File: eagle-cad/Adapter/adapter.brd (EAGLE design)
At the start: 55.8 x 65.1 mm, 19 parts, among them M1 WIREPADSMD5-2,5, M2 WIREPADSMD5-2,5, M3 WIREPADSMD5-2,5, M4 WIREPADSMD5-2,5

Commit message: Worked on Adapter
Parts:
- removed GND2, GND3, GND4, M1, M2, M3, M4, VBAT1, VBAT2, VBAT3, VBAT4: WIREPADSMD5-2,5, wirepad:5-2,5
- removed J4: (no value), SparkFun-Connectors:1X05_NO_SILK
- removed J5: (no value), SparkFun-Connectors:1X03_NO_SILK
- moved GND1 47.0 mm to (18.8, 5.10), turned to 180 degrees
- moved J1 26.1 mm to (18.7, 44.0), flipped to the bottom
- moved J2 22.4 mm to (34.0, 44.0), flipped to the bottom
- moved J3 9.87 mm to (33.2, 15.9), turned to 270 degrees
- moved VBAT 6.10 mm to (28.2, 5.03)
- moved GND 0.36 mm to (35.1, 5.14)
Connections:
- new net SBUS: GND1.1
- net 3V3: no longer J4.4
- net 5V: no longer J5.1
- net GND: no longer GND1.1, GND2.1, GND3.1, GND4.1, J4.5, J5.2
- net M1: no longer M1.1
- net M2: no longer M2.1
- net M3: no longer M3.1
- net M4: no longer M4.1
- net RX1: no longer J5.3
- net SCL: no longer J4.2
- net SDA: no longer J4.1
- net VBAT: no longer VBAT1.1, VBAT2.1, VBAT3.1, VBAT4.1
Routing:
- net VBAT: track 120.6 -> 0.00 mm
- net 5V: track 73.9 -> 0.14 mm, vias 1 -> 0
- net 3V3: track 50.5 -> 0.00 mm, vias 1 -> 0
- net M3: track 48.3 -> 0.00 mm, vias 1 -> 0
- net GND: track 46.8 -> 0.00 mm, vias 1 -> 0
- net M4: track 42.1 -> 0.00 mm, vias 1 -> 0
- net SDA: track 39.1 -> 0.00 mm
- net SCL: track 36.1 -> 0.00 mm
- net M1: track 29.6 -> 0.00 mm, vias 1 -> 0
- net RX1: track 16.4 -> 0.00 mm
- net M2: track 14.5 -> 0.00 mm, vias 1 -> 0
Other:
- board size 55.8 x 65.1 mm -> 34.5 x 48.1 mm
- board text removed: "+"
- board text removed: "3V3"
- board text removed: "5V"
- board text removed: "M1"
- board text removed: "M2"
- board text removed: "M3"
- board text removed: "M4"
- board text removed: "RX1"
- board text removed: "SCL"
- board text removed: "SDA"

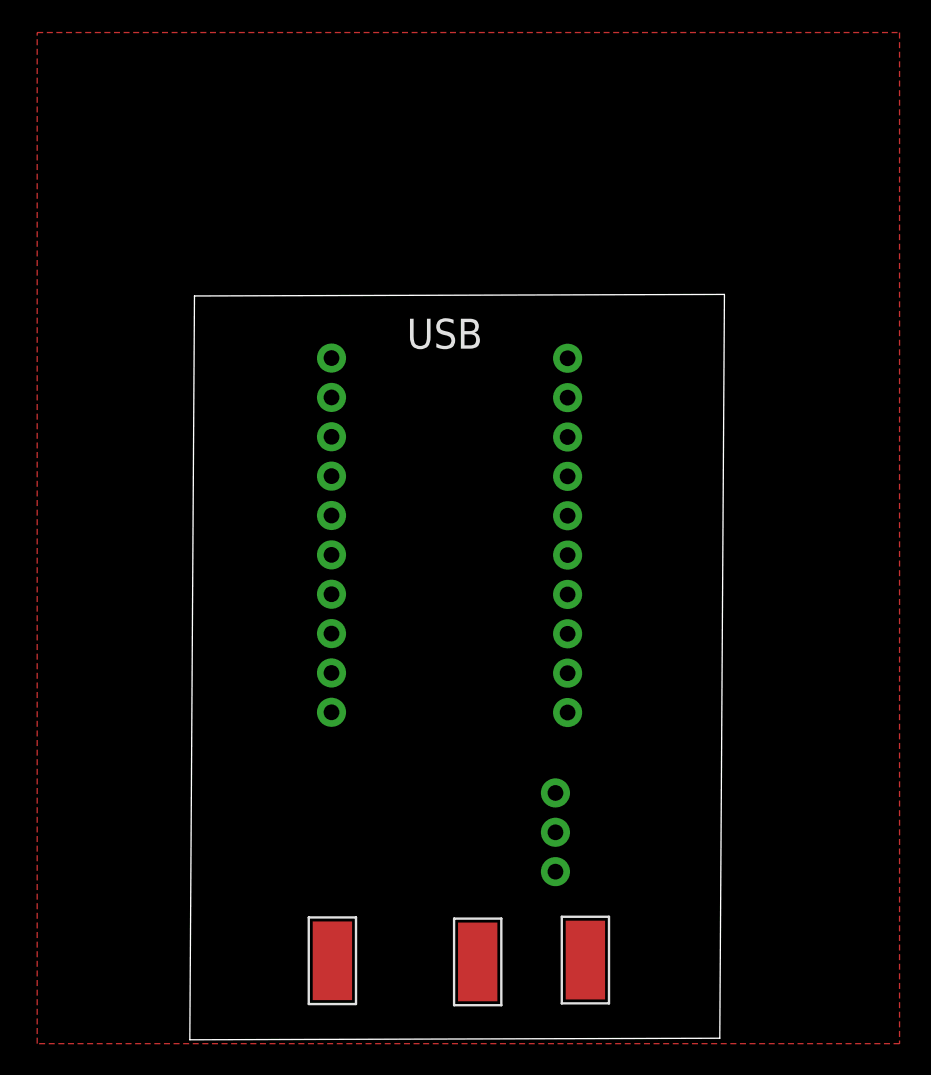
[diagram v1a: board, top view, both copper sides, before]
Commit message: Finished Taranis X-Lite adapter design
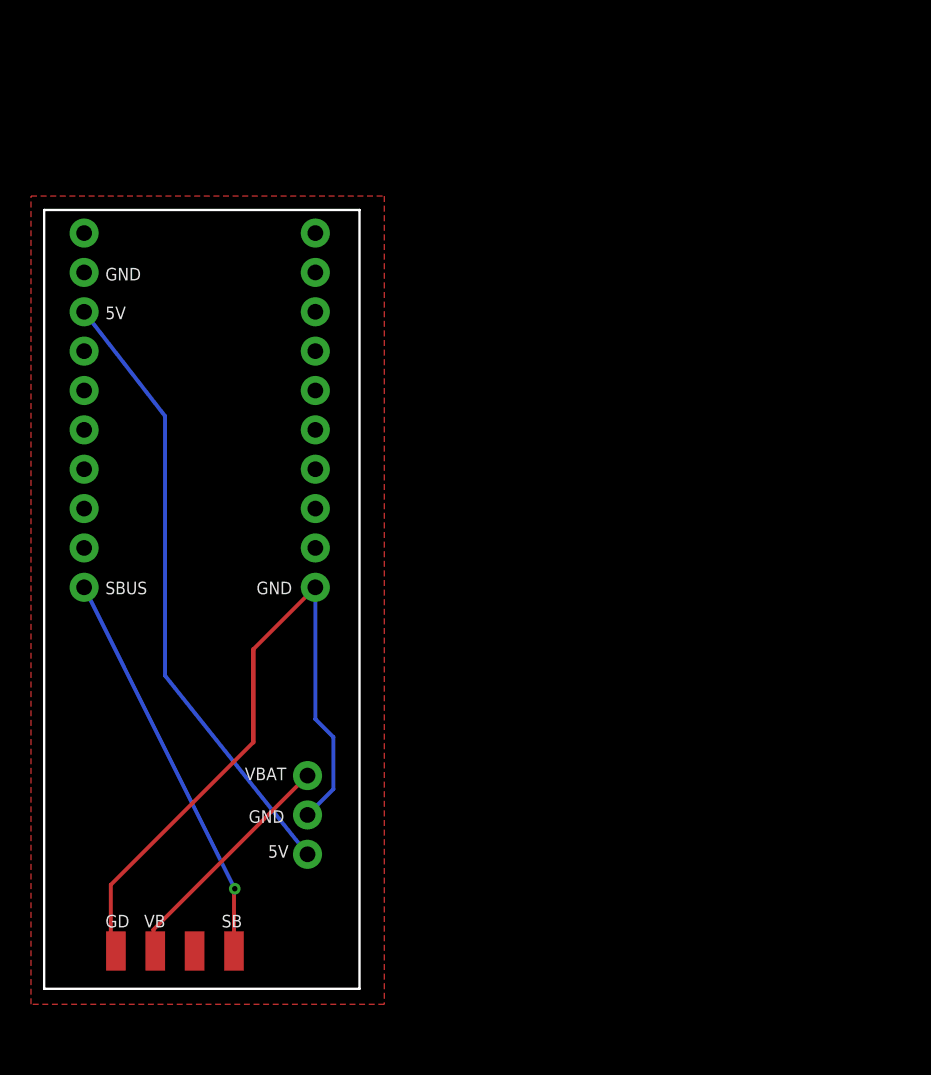
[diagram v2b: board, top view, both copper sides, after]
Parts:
- removed GND1: WIREPADSMD5-2,5, wirepad:5-2,5
- added PAD1, SBUS: (no value), wirepad:SMD1,27-2,54
- GND, VBAT: value WIREPADSMD5-2,5 -> (none); device wirepad:5-2,5 -> wirepad:SMD1,27-2,54
- moved J2 34.5 mm to (2.78, 29.2), turned to 90 degrees
- moved GND 30.3 mm to (4.83, 5.73)
- moved VBAT 20.8 mm to (7.37, 5.73)
- moved J3 16.5 mm to (17.2, 12.0), turned to 90 degrees
- moved J1 14.8 mm to (17.7, 29.2), turned to 90 degrees
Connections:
- removed net M1: J1.10
- removed net M4: J1.7
- removed net MISO: J2.2
- removed net MOSI: J2.1
- removed net RX1: J2.7
- removed net SCK: J2.3
- removed net SCL: J2.5
- removed net SDA: J2.6
- removed net SS: J2.4
- removed net TX1: J2.8
- net 5V: now also J2.8; no longer J1.3
- net GND: now also J1.1, J2.9; no longer J1.2, J2.10
- net SBUS: now also J2.1, SBUS.1; no longer GND1.1
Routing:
- net GND: track 0.00 -> 44.9 mm
- net 5V: track 0.14 -> 40.0 mm
- net SBUS: track 0.00 -> 26.3 mm, vias 0 -> 1
- net VBAT: track 0.00 -> 14.9 mm
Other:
- board size 34.5 x 48.1 mm -> 20.4 x 50.3 mm
- board text added: "5V"
- board text added: "GD"
- board text added: "GND"
- board text added: "SB"
- board text added: "SBUS"
- board text added: "VB"
- board text added: "VBAT"
- board text removed: "-"
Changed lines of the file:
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@@
 <?xml version="1.0" encoding="utf-8"?>
 <!DOCTYPE eagle SYSTEM "eagle.dtd">
-<eagle version="9.6.2">
+<eagle version="9.1.1">
 <drawing>
 <settings>
@@
 <setting verticaltext="up"/>
 </settings>
-<grid distance="0.1" unitdist="mm" unit="mm" style="lines" multiple="1" display="no" altdistance="5" altunitdist="mil" altunit="mil"/>
+<grid distance="9.84251969" unitdist="mil" unit="mil" style="lines" multiple="1" display="no" altdistance="5" altunitdist="mil" altunit="mil"/>
 <layers>
 <layer number="1" name="Top" color="4" fill="1" visible="yes" active="yes"/>
@@
 <board>
 <plain>
-<wire x1="9.6" y1="0" x2="43.8" y2="0.1" width="0" layer="20"/>
-<wire x1="43.8" y1="0.1" x2="44.1" y2="48.1" width="0" layer="20"/>
-<wire x1="44.1" y1="48.1" x2="9.9" y2="48" width="0" layer="20"/>
-<wire x1="9.9" y1="48" x2="9.6" y2="0" width="0" layer="20"/>
-<text x="23.6" y="44.6" size="1.9304" layer="25">USB</text>
-<text x="32.6" y="20.2" size="2.54" layer="26" rot="MR0">-</text>
+<text x="13.45" y="50.25" size="1.9304" layer="26" rot="MR0">USB</text>
+<wire x1="0.2" y1="53.55" x2="20.55" y2="53.55" width="0.1524" layer="20"/>
+<wire x1="20.55" y1="53.55" x2="20.55" y2="3.29" width="0.1524" layer="20"/>
+<wire x1="20.55" y1="3.29" x2="0.2" y2="3.29" width="0.1524" layer="20"/>
+<wire x1="0.2" y1="3.29" x2="0.2" y2="53.55" width="0.1524" layer="20"/>
+<text x="16.4" y="28.75" size="0.8128" layer="26" rot="MR0">GND</text>
+<text x="15.9" y="11.75" size="0.8128" layer="26" rot="MR0">5V</text>
+<text x="15.9" y="14" size="0.8128" layer="26" rot="MR0">GND</text>
+<text x="15.9" y="16.75" size="0.8128" layer="26" rot="MR0">VBAT</text>
+<text x="4.15" y="7.25" size="0.8128" layer="25">GD</text>
+<text x="6.65" y="7.25" size="0.8128" layer="25">VB</text>
+<text x="11.65" y="7.25" size="0.8128" layer="25">SB</text>
+<text x="4.15" y="28.75" size="0.8128" layer="25">SBUS</text>
+<text x="13.15" y="16.75" size="0.8128" layer="25">VBAT</text>
+<text x="13.4" y="14" size="0.8128" layer="25">GND</text>
+<text x="14.65" y="11.75" size="0.8128" layer="25">5V</text>
+<text x="4.15" y="46.5" size="0.8128" layer="25">5V</text>
+<text x="5.4" y="46.5" size="0.8128" layer="26" rot="MR0">5V</text>
+<text x="6.65" y="49" size="0.8128" layer="26" rot="MR0">GND</text>
+<text x="4.15" y="49" size="0.8128" layer="25">GND</text>
+<text x="13.9" y="28.75" size="0.8128" layer="25">GND</text>
+<text x="7.15" y="28.75" size="0.8128" layer="26" rot="MR0">SBUS</text>
 </plain>
 <attributes>
@@
 </autorouter>
 <elements>
-<element name="GND" library="wirepad" package="5-2,5" value="WIREPADSMD5-2,5" x="35.127490625" y="5.1442875" smashed="yes">
-<attribute name="VALUE" x="35.027490625" y="7.9442875" size="0.0254" layer="27"/>
-</element>
-<element name="VBAT" library="wirepad" package="5-2,5" value="WIREPADSMD5-2,5" x="28.177490625" y="5.02508125" smashed="yes">
-<attribute name="VALUE" x="28.077490625" y="7.82508125" size="0.0254" layer="27"/>
-</element>
-<element name="J1" library="SparkFun-Connectors" package="1X10_NO_SILK" value="" x="18.743490625" y="43.993071875" smashed="yes" rot="MR270">
-<attribute name="VALUE" x="20.775490625" y="45.263071875" size="0.6096" layer="28" font="vector" ratio="20" rot="MR270"/>
-</element>
-<element name="J2" library="SparkFun-Connectors" package="1X10_NO_SILK" value="" x="33.979040625" y="43.97908125" smashed="yes" rot="MR270">
-<attribute name="VALUE" x="36.011040625" y="45.24908125" size="0.6096" layer="28" font="vector" ratio="20" rot="MR270"/>
-</element>
-<element name="J3" library="SparkFun-Connectors" package="1X03_NO_SILK" value="" x="33.195209375" y="15.92935625" smashed="yes" rot="R270">
-<attribute name="VALUE" x="31.163209375" y="17.19935625" size="0.6096" layer="27" font="vector" ratio="20" rot="R270"/>
-</element>
-<element name="GND1" library="wirepad" package="5-2,5" value="WIREPADSMD5-2,5" x="18.8" y="5.1" smashed="yes" rot="R180">
-<attribute name="VALUE" x="18.9" y="2.3" size="0.0254" layer="27" rot="R180"/>
+<element name="J1" library="SparkFun-Connectors" package="1X10_NO_SILK" value="" x="17.7" y="29.2" smashed="yes" rot="MR90">
+<attribute name="VALUE" x="15.668" y="27.93" size="0.6096" layer="28" font="vector" ratio="20" rot="MR90"/>
+</element>
+<element name="J2" library="SparkFun-Connectors" package="1X10_NO_SILK" value="" x="2.779040625" y="29.2" smashed="yes" rot="MR90">
+<attribute name="VALUE" x="0.747040625" y="27.93" size="0.6096" layer="28" font="vector" ratio="20" rot="MR90"/>
+</element>
+<element name="J3" library="SparkFun-Connectors" package="1X03_NO_SILK" value="" x="17.195209375" y="11.96935625" smashed="yes" rot="R90">
+<attribute name="VALUE" x="19.227209375" y="10.69935625" size="0.6096" layer="27" font="vector" ratio="20" rot="R90"/>
+</element>
+<element name="GND" library="wirepad" package="SMD1,27-2,54" value="" x="4.83" y="5.73" smashed="yes">
+<attribute name="VALUE" x="4.83" y="5.73" size="0.0254" layer="27"/>
+</element>
+<element name="VBAT" library="wirepad" package="SMD1,27-2,54" value="" x="7.37" y="5.73" smashed="yes">
+<attribute name="VALUE" x="7.37" y="5.73" size="0.0254" layer="27"/>
+</element>
+<element name="SBUS" library="wirepad" package="SMD1,27-2,54" value="" x="12.45" y="5.73" smashed="yes">
+<attribute name="VALUE" x="12.45" y="5.73" size="0.0254" layer="27"/>
+</element>
+<element name="PAD1" library="wirepad" package="SMD1,27-2,54" value="" x="9.91" y="5.73" smashed="yes">
+<attribute name="VALUE" x="9.91" y="5.73" size="0.0254" layer="27"/>
 </element>
 </elements>
@@
 <signal name="GND">
 <polygon width="0.1524" layer="1">
-<vertex x="-0.25" y="65"/>
-<vertex x="55.4" y="65"/>
-<vertex x="55.4" y="-0.25"/>
-<vertex x="-0.25" y="-0.25"/>
+<vertex x="-0.65" y="54.45"/>
+<vertex x="22.15" y="54.45"/>
+<vertex x="22.15" y="2.29"/>
+<vertex x="-0.65" y="2.29"/>
 </polygon>
-<contactref element="J1" pad="2"/>
-<contactref element="J2" pad="10"/>
 <contactref element="J3" pad="2"/>
 <contactref element="GND" pad="1"/>
-<wire x1="33.979040625" y1="21.11908125" x2="18.743490625" y2="41.453071875" width="0" layer="19" extent="1-1"/>
-<wire x1="33.195209375" y1="13.38935625" x2="33.979040625" y2="21.11908125" width="0" layer="19" extent="1-1"/>
-<wire x1="35.127490625" y1="5.1442875" x2="33.195209375" y2="13.38935625" width="0" layer="19" extent="1-1"/>
+<contactref element="J1" pad="1"/>
+<contactref element="J2" pad="9"/>
+<wire x1="17.7" y1="29.2" x2="17.7" y2="20.6969375" width="0.254" layer="16"/>
+<wire x1="17.7" y1="20.6969375" x2="18.8636125" y2="19.533325" width="0.254" layer="16"/>
+<wire x1="18.8636125" y1="19.533325" x2="18.8636125" y2="16.177759375" width="0.254" layer="16"/>
+<wire x1="18.8636125" y1="16.177759375" x2="17.195209375" y2="14.50935625" width="0.254" layer="16"/>
+<wire x1="13.7" y1="25.2" x2="13.7" y2="19.2" width="0.3048" layer="1"/>
+<wire x1="13.7" y1="19.2" x2="4.5" y2="10" width="0.254" layer="1"/>
+<wire x1="4.5" y1="10" x2="4.5" y2="6.06" width="0.254" layer="1"/>
+<wire x1="4.5" y1="6.06" x2="4.83" y2="5.73" width="0.1524" layer="1"/>
+<wire x1="17.7" y1="29.2" x2="13.7" y2="25.2" width="0.254" layer="1"/>
 </signal>
 <signal name="5V">
-<contactref element="J1" pad="3"/>
 <contactref element="J3" pad="1"/>
-<wire x1="18.743490625" y1="38.913071875" x2="18.843490625" y2="39.013071875" width="0.1524" layer="16"/>
-<wire x1="33.195209375" y1="15.92935625" x2="18.743490625" y2="38.913071875" width="0" layer="19" extent="1-1"/>
+<contactref element="J2" pad="8"/>
+<wire x1="17.195209375" y1="11.96935625" x2="8" y2="23.5" width="0.254" layer="16"/>
+<wire x1="8" y1="23.5" x2="8" y2="40.25" width="0.254" layer="16"/>
+<wire x1="8" y1="40.25" x2="2.779040625" y2="46.98" width="0.254" layer="16"/>
 </signal>
 <signal name="3V3">
 <contactref element="J1" pad="4"/>
 </signal>
-<signal name="M1">
-<contactref element="J1" pad="10"/>
-</signal>
 <signal name="M2">
 <contactref element="J1" pad="9"/>
@@
 <signal name="M3">
 <contactref element="J1" pad="8"/>
-</signal>
-<signal name="M4">
-<contactref element="J1" pad="7"/>
-</signal>
-<signal name="SCL">
-<contactref element="J2" pad="5"/>
-</signal>
-<signal name="SDA">
-<contactref element="J2" pad="6"/>
-</signal>
-<signal name="SS">
-<contactref element="J2" pad="4"/>
-</signal>
-<signal name="SCK">
-<contactref element="J2" pad="3"/>
-</signal>
-<signal name="MISO">
-<contactref element="J2" pad="2"/>
-</signal>
-<signal name="MOSI">
-<contactref element="J2" pad="1"/>
-</signal>
-<signal name="RX1">
-<contactref element="J2" pad="7"/>
 </signal>
 <signal name="VBAT">
 <contactref element="J3" pad="3"/>
 <contactref element="VBAT" pad="1"/>
-<wire x1="28.177490625" y1="5.02508125" x2="33.195209375" y2="10.84935625" width="0" layer="19" extent="1-1"/>
-</signal>
-<signal name="TX1">
-<contactref element="J2" pad="8"/>
+<wire x1="17.195209375" y1="17.04935625" x2="7.25" y2="7.104146875" width="0.254" layer="1"/>
+<wire x1="7.25" y1="7.104146875" x2="7.25" y2="6.25" width="0.254" layer="1"/>
+<wire x1="7.25" y1="6.25" x2="7.37" y2="5.73" width="0" layer="19" extent="1-1"/>
 </signal>
 <signal name="SBUS">
-<contactref element="GND1" pad="1"/>
+<contactref element="SBUS" pad="1"/>
+<contactref element="J2" pad="1"/>
+<wire x1="12.45" y1="5.73" x2="12.45" y2="9.95" width="0.254" layer="1"/>
+<wire x1="12.45" y1="9.95" x2="12.5" y2="10" width="0.1524" layer="1"/>
+<wire x1="12.5" y1="10" x2="12.5" y2="9.75" width="0.1524" layer="1"/>
+<via x="12.5" y="9.75" extent="1-16" drill="0.35"/>
+<wire x1="12.5" y1="9.75" x2="2.779040625" y2="29.2" width="0.254" layer="16"/>
 </signal>
 </signals>
